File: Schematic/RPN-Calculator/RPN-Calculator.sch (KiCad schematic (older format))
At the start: 33 parts

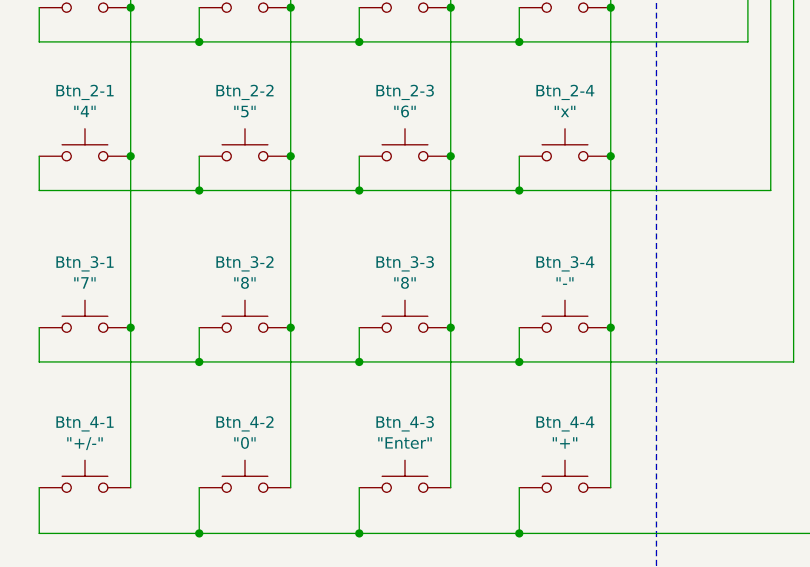
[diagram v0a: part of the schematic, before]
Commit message: Correct schematic button label '9'
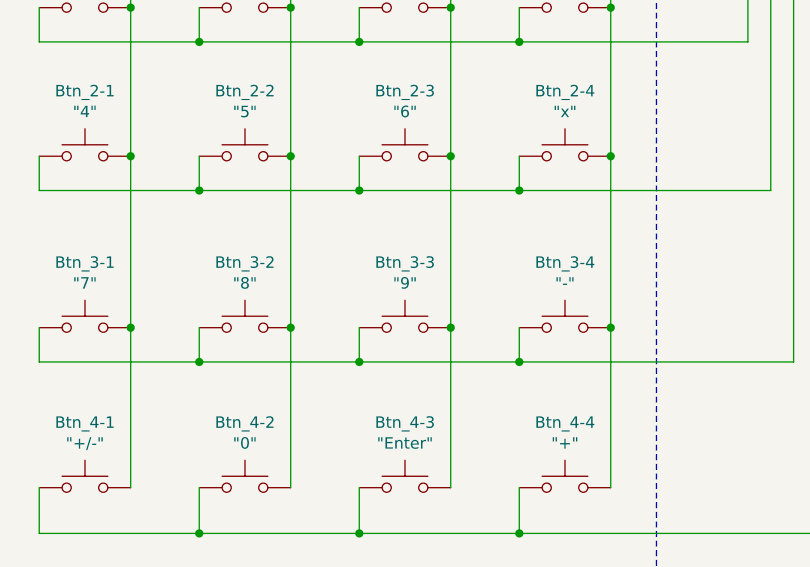
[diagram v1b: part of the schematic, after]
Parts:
- Btn_3-3: value \"8\" -> \"9\"
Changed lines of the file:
@@
 P 4050 6650
 F 0 "Btn_3-3" H 4050 6935 50  0000 C CNN
-F 1 "\"8\"" H 4050 6844 50  0000 C CNN
+F 1 "\"9\"" H 4050 6844 50  0000 C CNN
 F 2 "" H 4050 6850 50  0001 C CNN
 F 3 "~" H 4050 6850 50  0001 C CNN
